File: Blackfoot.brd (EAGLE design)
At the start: 50.7 x 29.1 mm, 60 parts, among them IC1 ATMEGA644M, J1 CONN_4SCREW_2.54, J2 CONN_6, Q1 MOSFET_PCH-IRLML2244, Q2 MOSFET-NCH-DMG3404L, Q5 MOSFET_PCH-IRLML2244, U2 FT231X-Q

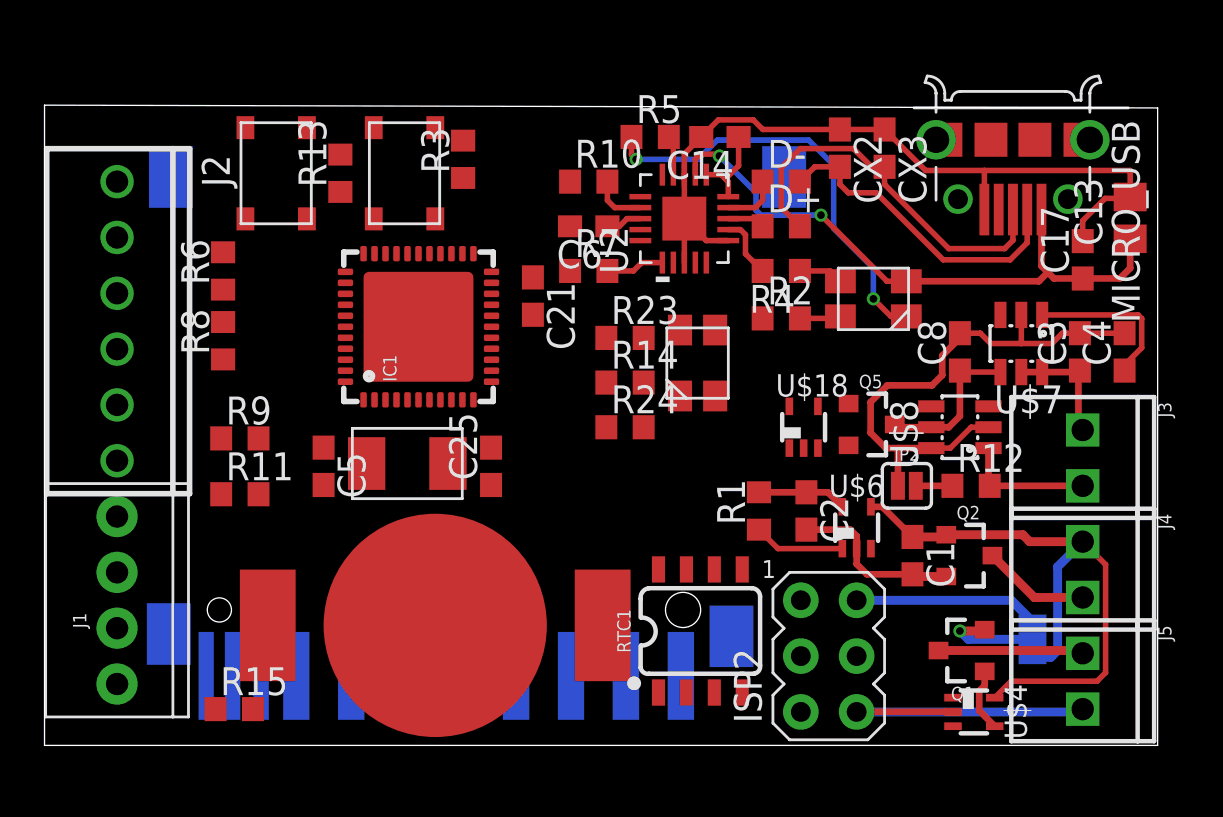
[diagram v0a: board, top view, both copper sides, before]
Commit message: Preliminary layout done, fixed led issue
Finished with first round layout, changed supply voltage for LEDs to be 3v3 instead of VUSB so that alive led can work regardless of use of USB voltage
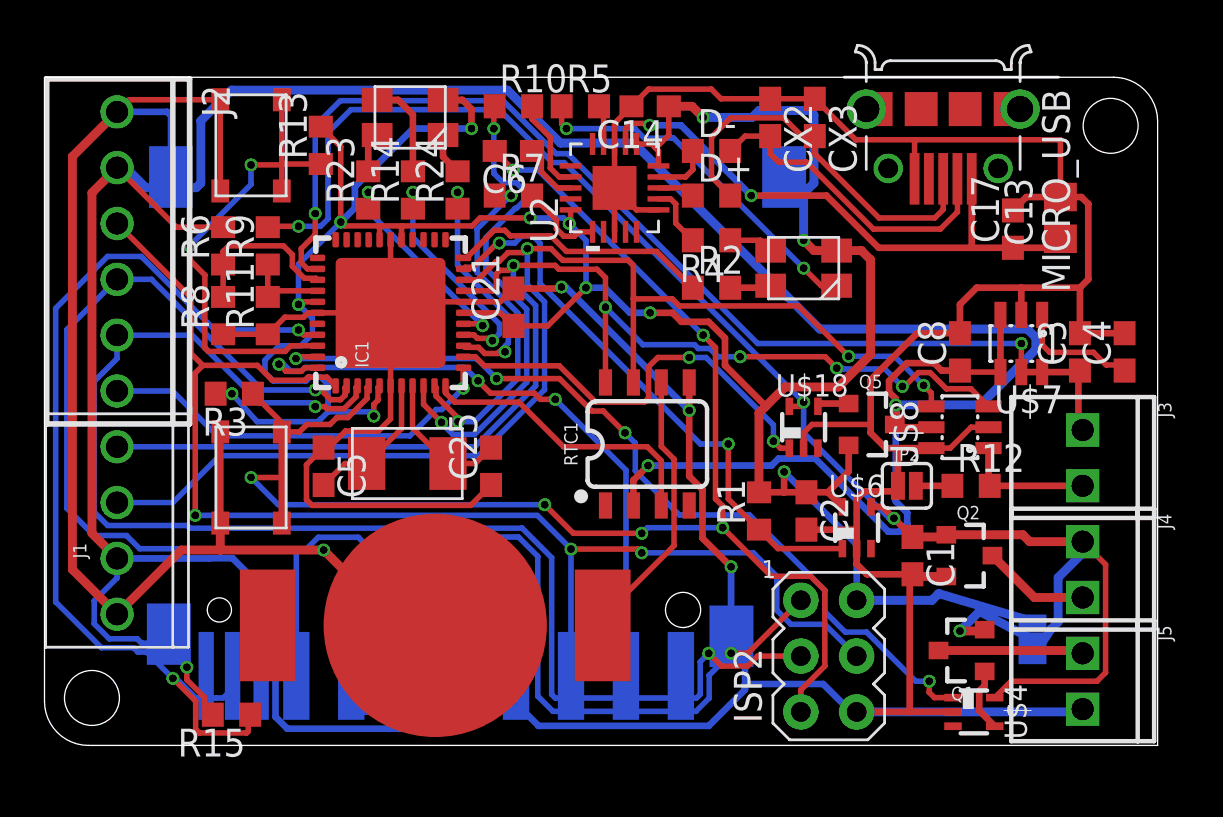
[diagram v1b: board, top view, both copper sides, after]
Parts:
- moved U$15 17.2 mm to (16.6, 28.6), turned to 180 degrees
- moved U$9 15.5 mm to (9.40, 12.2)
- moved R3 14.9 mm to (8.64, 16.0), turned to 180 degrees
- moved R23 13.5 mm to (14.7, 25.3), turned to 90 degrees
- moved R24 13.2 mm to (18.8, 25.3), turned to 90 degrees
- moved R14 13.0 mm to (16.8, 25.3), turned to 90 degrees
- moved R9 8.85 mm to (10.2, 22.7), turned to 90 degrees
- moved RTC1 8.84 mm to (27.4, 13.7)
- moved R11 8.23 mm to (10.2, 19.6), turned to 90 degrees
- moved C6 4.85 mm to (21.3, 27.1)
- moved R10 4.85 mm to (21.3, 29.1)
- moved R7 4.85 mm to (21.3, 25.0)
- moved MICRO_USB 3.47 mm to (40.9, 29.0)
- moved U$16 3.47 mm to (34.5, 21.7)
- moved C14 3.47 mm to (27.6, 29.1)
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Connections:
- removed net SC_CD: R15.1, U$3.CD
- net 3.3V_EXT_CTRL: now also IC1.13
- net 3V3: now also U$16.2; no longer R6.2
- net EXT_3.3V: now also R6.2
- net SD_CD: now also R15.1, U$3.CD
- net SD_CS: now also IC1.44; no longer IC1.43
- net VSWITCH_CTRL: now also IC1.43; no longer IC1.44
- net VUSB: no longer U$16.2
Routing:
- net GND: track 82.8 -> 275.2 mm, vias 0 -> 4
- net EXT_3.3V: track 7.17 -> 151.4 mm, vias 0 -> 3
- net 3V3: track 16.4 -> 131.0 mm, vias 0 -> 12
- net MISO: track 0.00 -> 87.4 mm, vias 0 -> 2
- net SCK: track 0.00 -> 69.7 mm, vias 0 -> 2
- net RST: track 0.00 -> 69.5 mm, vias 0 -> 6
- net MOSI: track 0.00 -> 61.0 mm, vias 0 -> 3
- net SCL: track 0.00 -> 58.2 mm, vias 0 -> 5
- net SDA: track 0.00 -> 58.2 mm, vias 0 -> 3
- net VREF: track 5.41 -> 51.2 mm, vias 0 -> 2
- net SD_CD: track 0.00 -> 44.4 mm, vias 0 -> 2
- net VBAT+: track 29.0 -> 70.6 mm, vias 0 -> 3
- net VSWITCH_CTRL: track 0.00 -> 38.9 mm, vias 0 -> 4
- net SD_CS: track 0.00 -> 29.3 mm, vias 0 -> 3
- net LOG_INT: track 0.00 -> 22.4 mm, vias 0 -> 2
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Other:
- board size 50.7 x 29.1 mm -> 50.7 x 30.4 mm

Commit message: Edits for 0.1"compatability
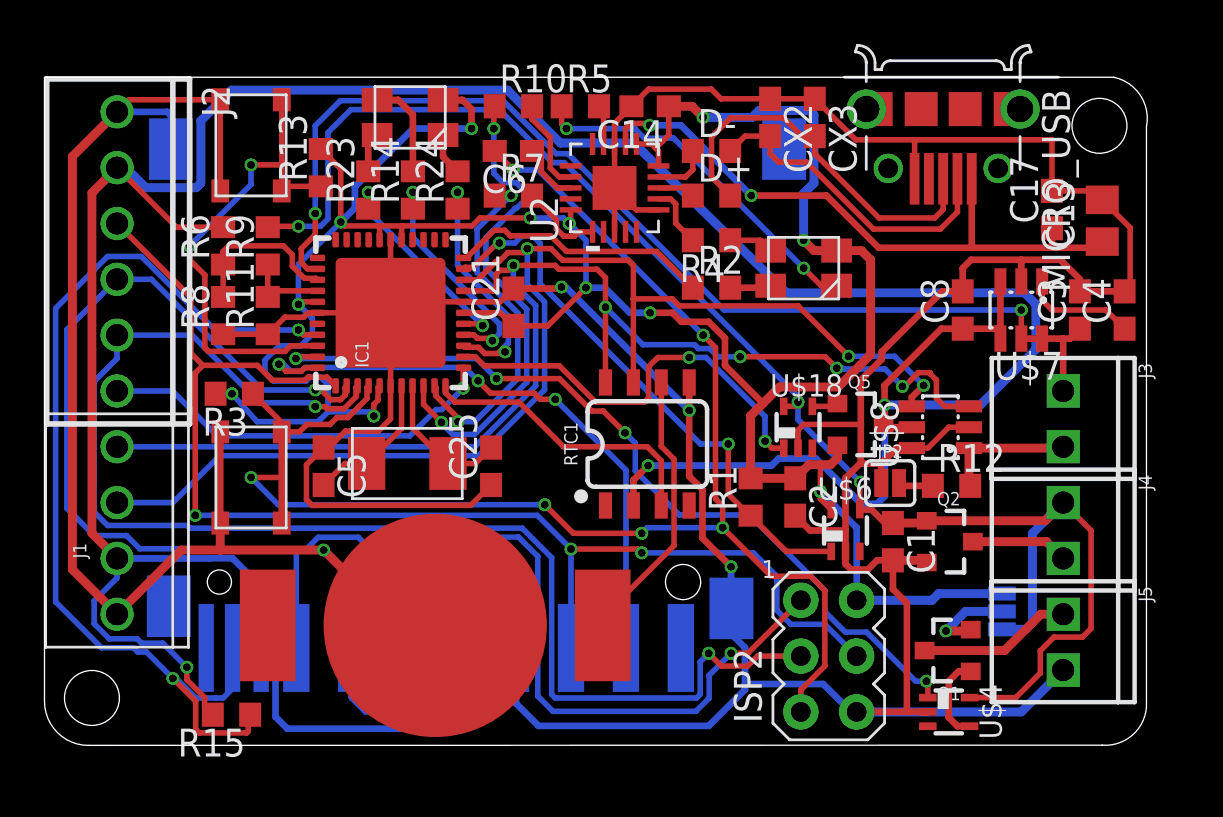
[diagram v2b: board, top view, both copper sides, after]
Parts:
- added U$2: (no value), awickert:NWLOGO_MED
- moved J3 1.99 mm to (46.4, 16.1)
- moved J5 1.99 mm to (46.4, 5.97)
- moved J4 1.99 mm to (46.4, 11.0)
- moved C17 1.99 mm to (45.8, 24.4)
- moved C8 1.91 mm to (41.8, 19.8)
- moved C13 1.91 mm to (48.1, 23.9)
- moved C3 1.91 mm to (47.1, 19.8)
- moved C4 1.91 mm to (49.1, 19.8)
- moved JP1 1.89 mm to (43.6, 6.10)
- moved U$7 1.52 mm to (44.5, 19.8)
- moved U$3 1.27 mm to (19.6, 5.33)
- moved U$4 1.14 mm to (41.1, 1.52)
- moved C1 1.09 mm to (38.6, 9.27)
- moved Q2 1.09 mm to (41.1, 9.27)
- moved R13 1.02 mm to (12.6, 26.3)
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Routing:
- net GND: track 275.2 -> 269.5 mm
- net 3V3: track 131.0 -> 125.9 mm
- net VUSB: track 26.2 -> 29.0 mm
- net VBAT+: track 70.6 -> 72.7 mm
- net MOSI: track 61.0 -> 59.7 mm
- net SD_CD: track 44.4 -> 45.6 mm
- net SD_CS: track 29.3 -> 28.0 mm
- net MISO: track 87.4 -> 86.1 mm
- net SCK: track 69.7 -> 68.4 mm
- net N$2: track 2.89 -> 3.95 mm
- net VSWITCH_CTRL: track 38.9 -> 37.9 mm
- net N$3: track 5.14 -> 4.19 mm
- net VREF: track 51.2 -> 50.4 mm
- net N$11: track 5.74 -> 5.14 mm
- net PG: track 26.3 -> 25.7 mm
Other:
- board size 50.7 x 30.4 mm -> 50.2 x 30.4 mm
- board text added: "3v3"
- board text added: "AUX"
- board text added: "Ax"
- board text added: "B+"
- board text added: "B-"
- board text added: "CS"
- board text added: "DI"
- board text added: "DO"
- board text added: "GND"
- board text added: "J0"
- board text added: "J1"
- board text added: "LOG"
- board text added: "Project Blackfoot v0.0 ---------------- Developed by Northern Widget and University of Minnesota"
- board text added: "REF"
- board text added: "RST"
- board text added: "SCK"
- board text added: "SCL"
- board text added: "SDA"
- board text added: "STAT"
- board text added: "VBat"
- board text added: "Vs"

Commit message: Minor edits, generated gerbers
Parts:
- moved U$2 1.27 mm to (38.1, 16.5)
- moved BT1 0.13 mm to (17.8, 5.59)
